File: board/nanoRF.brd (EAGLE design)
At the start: 22.9 x 49.5 mm, 25 parts

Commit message: edge
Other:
- board size 22.9 x 49.5 mm -> 20.3 x 49.5 mm
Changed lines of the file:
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@@
 <board>
 <plain>
-<wire x1="-2.54" y1="0" x2="20.32" y2="0" width="0" layer="20"/>
-<wire x1="20.32" y1="0" x2="20.32" y2="49.53" width="0" layer="20"/>
-<wire x1="20.32" y1="49.53" x2="-2.54" y2="49.53" width="0" layer="20"/>
-<wire x1="-2.54" y1="49.53" x2="-2.54" y2="0" width="0" layer="20"/>
+<wire x1="-1.27" y1="0" x2="19.05" y2="0" width="0" layer="20"/>
+<wire x1="19.05" y1="0" x2="19.05" y2="49.53" width="0" layer="20"/>
+<wire x1="19.05" y1="49.53" x2="-1.27" y2="49.53" width="0" layer="20"/>
+<wire x1="-1.27" y1="49.53" x2="-1.27" y2="0" width="0" layer="20"/>
 <text x="14.0208" y="11.7884" size="0.8128" layer="21" rot="SR45" align="top-left">TX</text>
 <text x="13.97" y="13.9982" size="0.8128" layer="21" rot="SR45" align="top-left">RX</text>
@@
 <contactref element="RF24" pad="6"/>
 <polygon width="0.2032" layer="1">
-<vertex x="-2.54" y="50.038"/>
-<vertex x="-2.54" y="0"/>
-<vertex x="20.447" y="0"/>
-<vertex x="20.4216" y="50.0126"/>
+<vertex x="-1.905" y="50.038"/>
+<vertex x="-1.905" y="0"/>
+<vertex x="19.812" y="0"/>
+<vertex x="19.7866" y="50.0126"/>
 </polygon>
 <wire x1="16.51" y1="20.32" x2="9.525" y2="20.32" width="0.2032" layer="1"/>
@@
 <wire x1="9.017" y1="33.528" x2="8.89" y2="33.401" width="0.2032" layer="1"/>
 <polygon width="0.2032" layer="16">
-<vertex x="-2.54" y="50.292"/>
-<vertex x="-2.54" y="0"/>
-<vertex x="20.447" y="0"/>
-<vertex x="20.4978" y="50.3682"/>
+<vertex x="-1.905" y="50.292"/>
+<vertex x="-1.905" y="0"/>
+<vertex x="19.812" y="0"/>
+<vertex x="19.8628" y="50.3682"/>
 </polygon>
 <wire x1="8.89" y1="33.401" x2="8.89" y2="33.02" width="0.3048" layer="1"/>

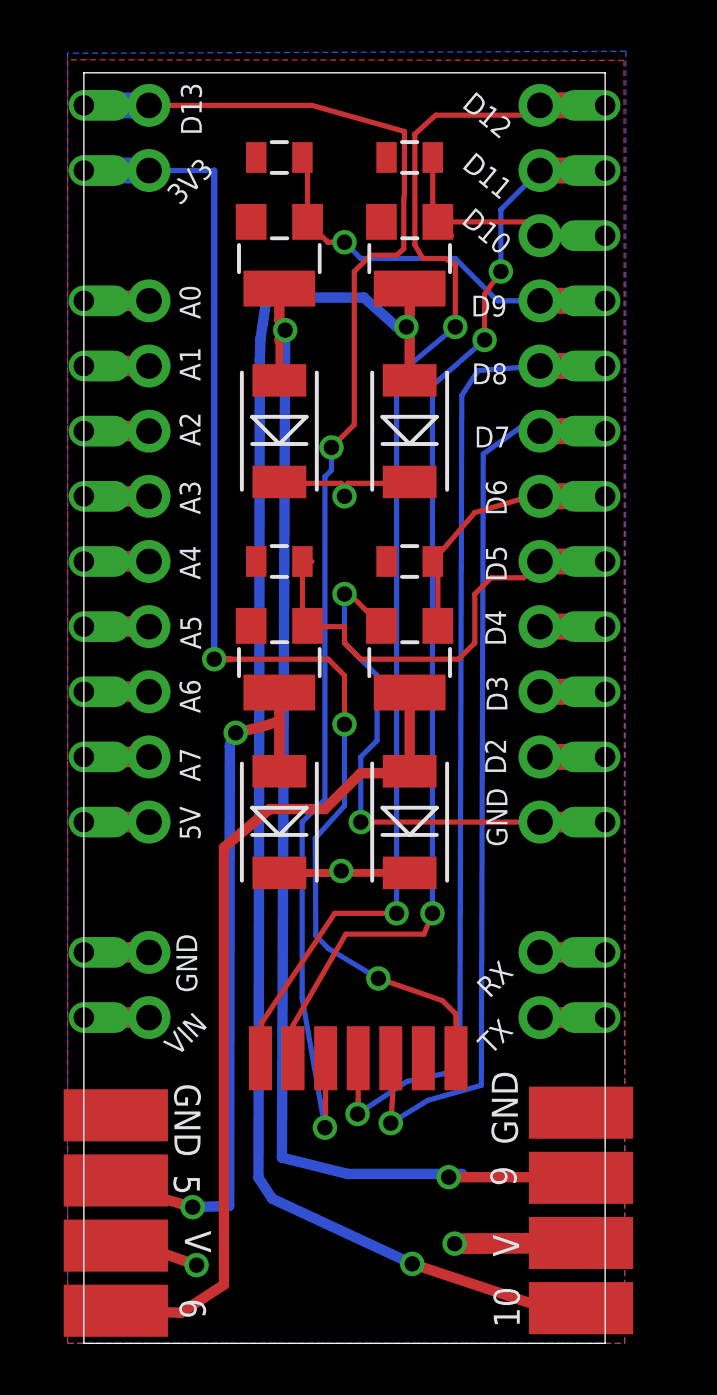
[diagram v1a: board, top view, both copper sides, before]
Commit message: added noEdge
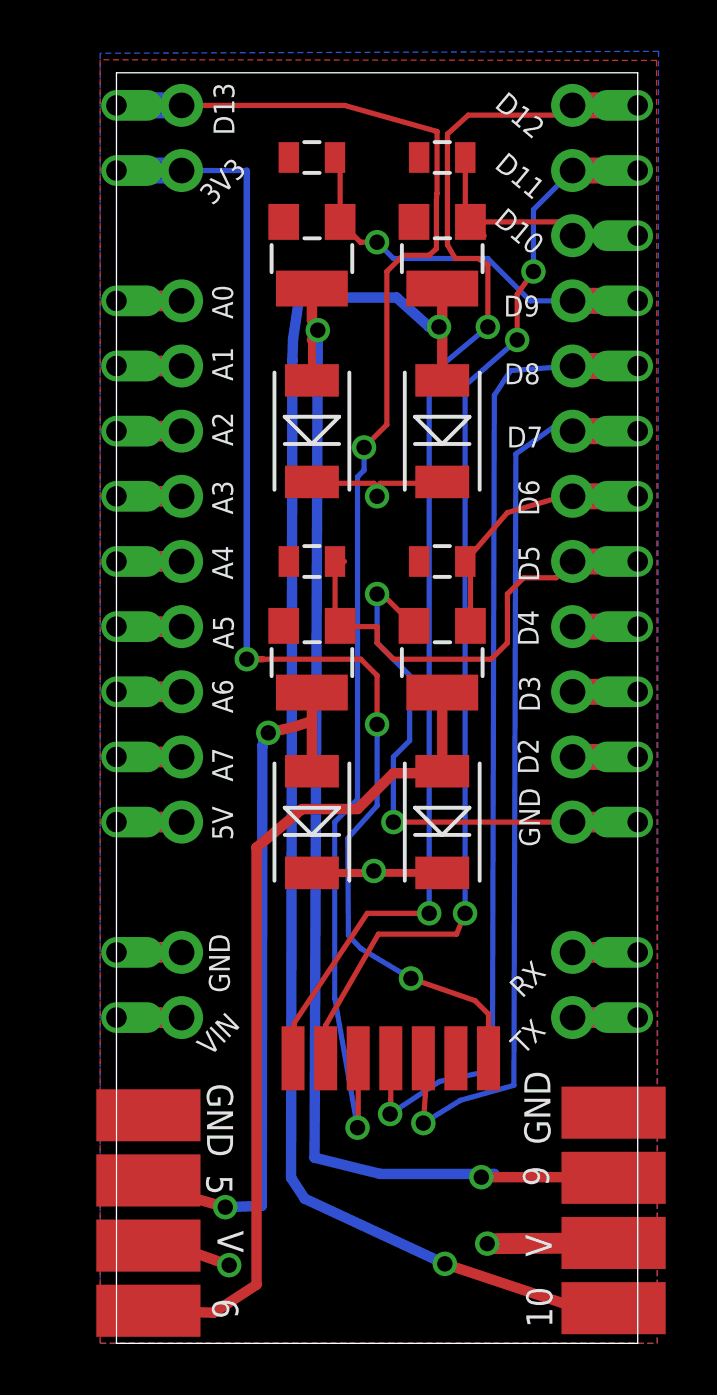
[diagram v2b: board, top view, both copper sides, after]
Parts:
- moved D2 1.27 mm to (7.62, 20.3)
- moved D4 1.27 mm to (7.62, 35.6)
- moved Q2 1.27 mm to (7.62, 26.7)
- moved Q4 1.27 mm to (7.62, 42.4)
- moved R4 1.27 mm to (7.62, 30.5)
- moved R6 1.27 mm to (7.62, 46.2)
- moved MOSFET-12 1.27 mm to (1.24, 5.08)
- moved RF24 1.27 mm to (4.06, 11.3)
- moved U$11 1.27 mm to (2.54, 47.0)
- moved U$12 1.27 mm to (2.54, 14.0)
- moved U$13 1.27 mm to (0.00, 14.0)
- moved U$6 1.27 mm to (2.54, 30.5)
- moved U$7 1.27 mm to (0.00, 30.5)
- moved U$8 1.27 mm to (0.00, 47.0)
- moved D1 1.27 mm to (12.7, 20.3)
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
